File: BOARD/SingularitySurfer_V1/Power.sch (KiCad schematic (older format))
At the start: 32 parts, among them J1 USB_B_Micro, SW1 SW_DIP_x01, U1 BD81870EFV, U2 MIC5504-3.3YM5, U3 TLV70212_SOT23-5

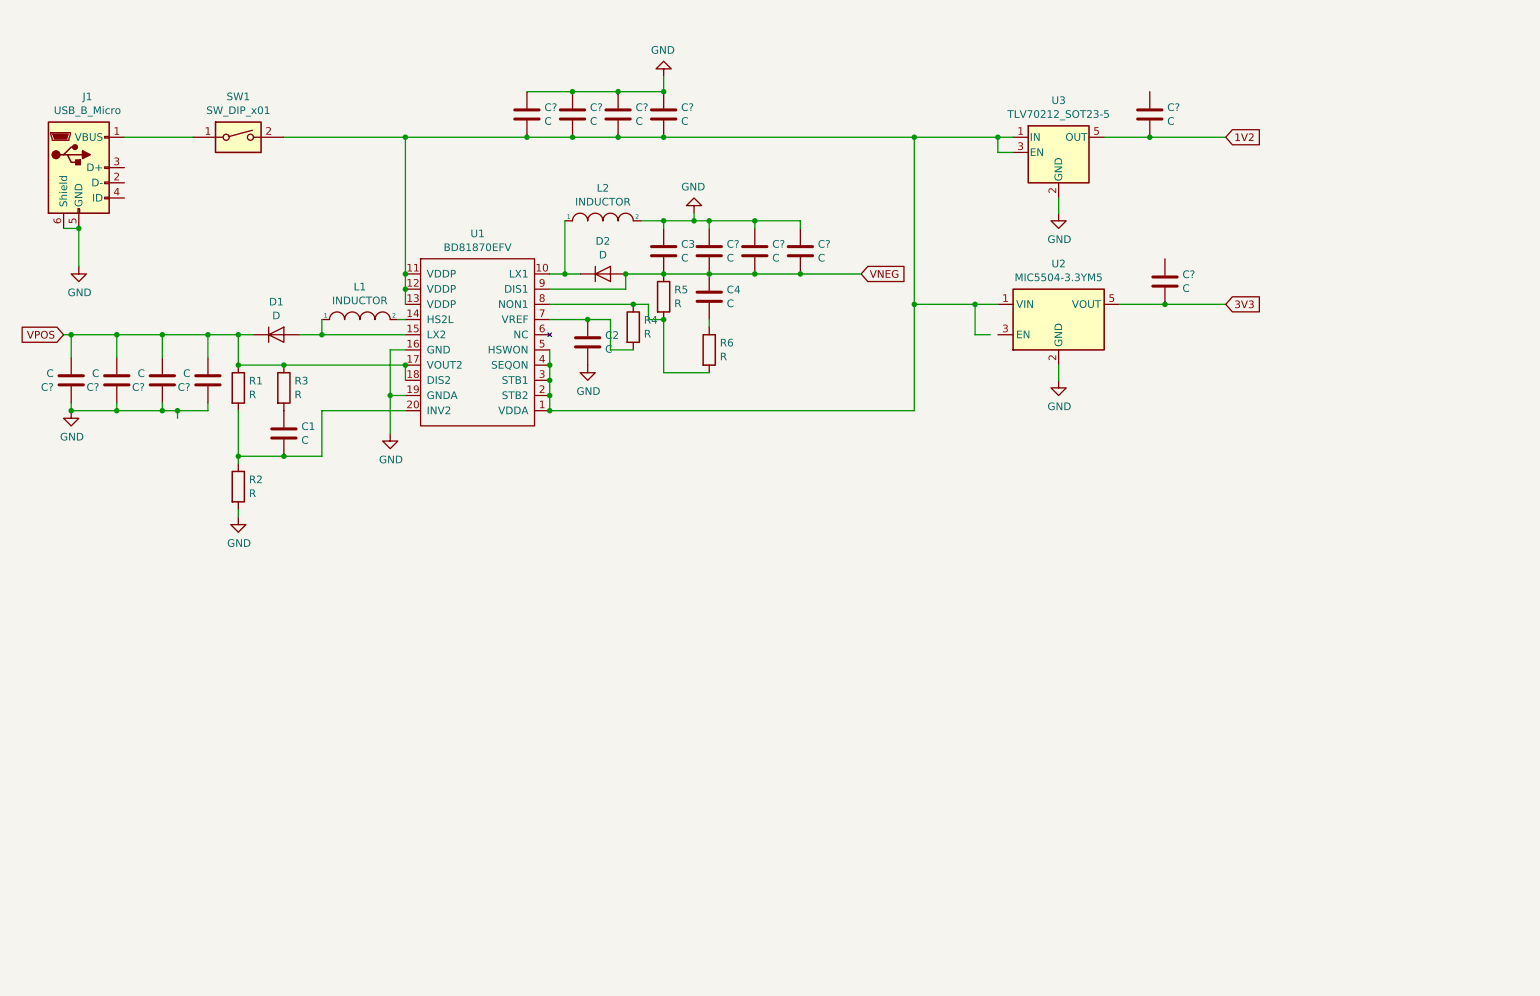
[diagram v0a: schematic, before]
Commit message: More work on final Schematic. Power, digital and output section close to final. No frontend yet.
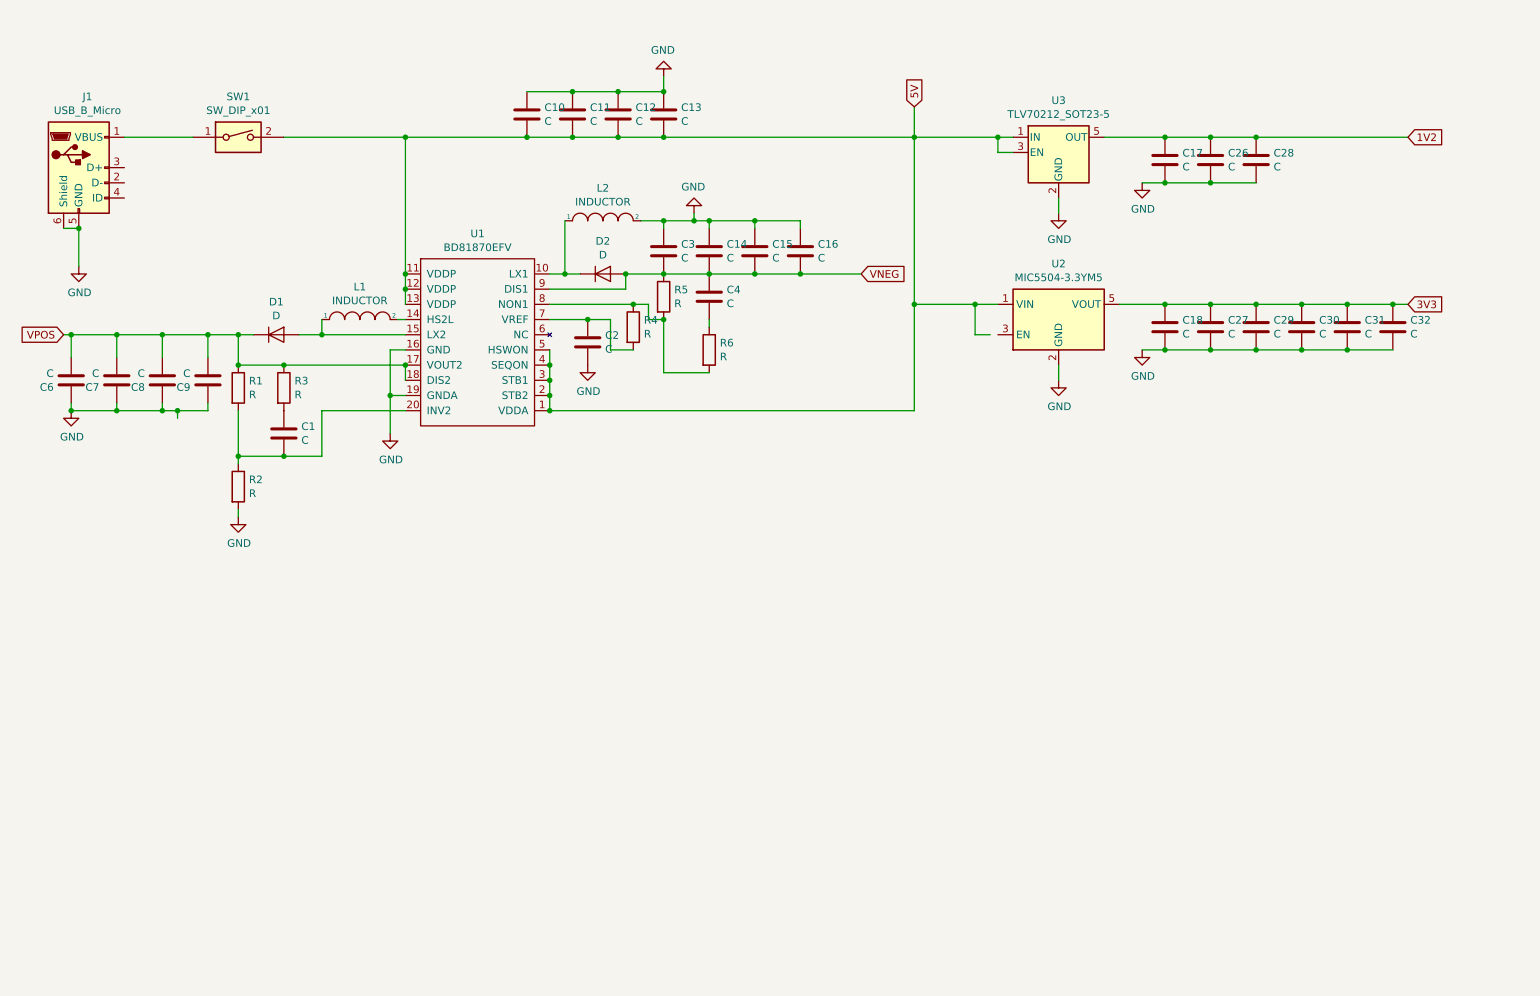
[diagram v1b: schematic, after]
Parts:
- added C26, C27, C28, C29, C30, C31, C32: C, symbol Device:C
- U1: footprint Button_Switch_THT:SW_CuK_JS202011AQN_DPDT_Angled -> Package_SO:SSOP-20_4.4x6.5mm_P0.65mm
- U2, U3: footprint Package_TO_SOT_SMD:SOT-23-5 -> Package_TO_SOT_SMD:SOT-23-5_HandSoldering
- gave numbers to parts that had none: 13
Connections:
- net 1V2: now also C17.1, C26.1, C28.1; no longer C17.2
- net 3V3: now also C18.1, C27.1, C29.1, C30.1, C31.1, C32.1; no longer C18.2
- net GND: now also C17.2, C18.2, C26.2, C27.2, C28.2, C29.2, C30.2, C31.2, C32.2
- net 5V: now reaches C10.2, C11.2, C12.2, C13.2, SW1.2, U1.1 (VDDA), U1.11 (VDDP), U1.12 (VDDP), U1.13 (VDDP), U1.2 (STB2), U1.3 (STB1), U1.4 (SEQON), U1.5 (HSWON), U2.1 (VIN), U3.1 (IN), U3.3 (EN)
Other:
- moved on the sheet: C17, C18

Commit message: Final Board schematic almost done and started on layout
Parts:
- added C43, C51: C, Capacitor_SMD:C_1206_3216Metric_Pad1.42x1.75mm_HandSolder, symbol Device:C
- added C44, C45, C46, C47, C48, C49, C50, C52, C53, C54, C55, C56: C, Capacitor_SMD:C_0805_2012Metric_Pad1.15x1.40mm_HandSolder, symbol Device:C
- added D16: D_Zener, Diode_SMD:D_SOD-323, symbol Device:D_Zener
- added D17: D_Schottky_x2_Serial_AKC, Package_TO_SOT_SMD:SOT-23, symbol Device:D_Schottky_x2_Serial_AKC
- added D3001: LED, LED_SMD:LED_0805_2012Metric_Pad1.15x1.40mm_HandSolder, symbol Device:LED
- added R35, R36, R37, R38: R, Resistor_SMD:R_0805_2012Metric_Pad1.15x1.40mm_HandSolder, symbol Device:R
- added U13: LT3032, Package_DFN_QFN:Linear_DE14MA, symbol Regulator_Linear:LT3032
- added U14: AP2114-1.8, Package_TO_SOT_SMD:TO-252-3_TabPin2, symbol SingularitySurfer:AP2114-1.8
- C1, C4: footprint (none) -> Capacitor_SMD:C_1206_3216Metric_Pad1.42x1.75mm_HandSolder
- C10, C11, C12, C13, C14, C15, C16, C17, C18, C2, C26, C27, C28, C29, C3, C30, C31, C32, C6, C7, C8, C9: footprint (none) -> Capacitor_SMD:C_0805_2012Metric_Pad1.15x1.40mm_HandSolder
- D1, D2: footprint (none) -> Diode_SMD:D_2010_5025Metric_Pad1.52x2.65mm_HandSolder
- L1, L2: footprint (none) -> Inductor_SMD:L_Taiyo-Yuden_NR-40xx_HandSoldering
- R1, R2, R3, R4, R5, R6: footprint (none) -> Resistor_SMD:R_0805_2012Metric_Pad1.15x1.40mm_HandSolder
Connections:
- net 5V: now also D16.1 (K), D3001.2 (A)
- net GND: now also C44.2, C45.2, C46.2, C47.2, C48.2, C49.2, C50.2, C52.2, C53.2, C54.2, C55.2, C56.2, D16.2 (A), D17.1 (A), D3001.1 (K), R36.1, R38.1, U13.4 (GND), U13.5 (GND), U14.2 (GND)
- net VPOS: now also U13.10 (~SHDNN), U13.12 (~SHDNP), U13.14 (INP)
- net VNEG: no longer names the net of C14.2, C15.2, C16.2, C3.2, C4.1, D2.2 (A), R5.1, U1.9 (DIS1)
- net VNEG: now also U13.6 (INN), U13.9 (INN)
- new net: R35.1, R36.2, U13.2 (ADJP)
- new net: C43.2, U13.3 (BYPP)
- new net: C51.2, U13.11 (BYPN)
- new net: R37.1, R38.2, U13.8 (ADJN)
- new net +8V: C43.1, C44.1, C46.1, C48.1, C49.1, C50.1, R35.2, U13.1 (OUTP), U14.1 (VIN)
- new net -8V: C51.1, C52.1, C53.1, C54.1, C55.1, C56.1, U13.7 (OUTN)
- new net A1V8: C45.1, C47.1, U14.3 (VOUT)
- no-connect marks 0 -> 1

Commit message: SignularitiSurfer final boar almost donegit status! Fuuuak this is getting rediculous...
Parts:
- added C57, C58, C59, C60, C64: C, Capacitor_SMD:C_0805_2012Metric_Pad1.15x1.40mm_HandSolder, symbol Device:C
- added C61, C62, C63: C, Capacitor_SMD:C_0402_1005Metric, symbol Device:C
- added J13, J14: Conn_01x03, Connector_JST:JST_EH_B3B-EH-A_1x03_P2.50mm_Vertical, symbol Connector_Generic:Conn_01x03
- added R39: R, Resistor_SMD:R_0805_2012Metric_Pad1.15x1.40mm_HandSolder, symbol Device:R
- added TP1, TP2, TP3, TP4, TP5, TP6, TP7, TP8: TestPoint, TestPoint:TestPoint_Keystone_5000-5004_Miniature, symbol Connector:TestPoint
- C30, C52: footprint Capacitor_SMD:C_0805_2012Metric_Pad1.15x1.40mm_HandSolder -> Capacitor_SMD:C_0402_1005Metric
- U13: footprint Package_DFN_QFN:Linear_DE14MA -> SingularitySurfer:DFN-14-1EP_split_bottom_pad_3x4mm_P0.5mm_EP1.7x3.3mm
- renumbered D3001 to D18
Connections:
- net +8V: now also C59.1, J13.1 (Pin_1), J14.1 (Pin_1), TP4.1
- net -8V: now also R37.2, C60.1, J13.3 (Pin_3), J14.3 (Pin_3), TP7.1; no longer C52.1
- net 1V2: now also C52.1, C62.1, TP8.1
- net 3V3: now also C61.1, C63.1, C64.1, TP6.1
- net 5V: now also D17.3 (common), C57.2, C58.2
- net GND: now also C57.1, C58.1, C59.2, C60.2, C61.2, C62.2, C63.2, C64.2, J13.2 (Pin_2), J14.2 (Pin_2), R39.1; no longer D18.1 (K)
- net VPOS: now also TP1.1
- net at J1.1 (VBUS), SW1.1: now also TP2.1
- net VNEG: now reaches C14.2, C15.2, C16.2, C3.2, C4.1, D2.2 (A), R5.1, U1.9 (DIS1), U13.6 (INN), U13.9 (INN)
- net VNEG: now also TP5.1
- net A1V8 renamed 1V8
- net 1V8: now also TP3.1
- new net: D18.1 (K), R39.2
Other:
- moved on the sheet: C44, C45, C46, C47, C48, C49, C50, U14

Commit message: Final board done, plotted and in production. Started on LCD driver, already working with scrolling HI :)
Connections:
- net 5V: now also U2.3 (EN)
- no-connect marks 1 -> 4
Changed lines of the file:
@@
 	7000 2700 7000 3400
-Wire Wire Line
-	7500 2900 7400 2900
 Wire Wire Line
 	7400 2900 7400 2700
@@
 $EndComp
 Wire Wire Line
-	6650 2500 6650 5150
-Wire Wire Line
 	1150 2900 1150 5250
 Wire Wire Line
@@
 Text Label 1150 5250 0    50   ~ 0
 VPOS
-Text GLabel 6350 5350 0    50   Input ~ 0
-VPOS
-Wire Wire Line
-	6350 5350 6650 5350
 $Comp
 L power:GND #PWR0151
@@
 	10450 3000 10750 3000
 Connection ~ 10450 3000
+Wire Wire Line
+	6650 2500 6650 5150
+Wire Wire Line
+	6650 5350 6650 6000
+Wire Wire Line
+	6650 6000 1150 6000
+Wire Wire Line
+	1150 6000 1150 5250
+Connection ~ 1150 5250
+NoConn ~ 1800 1800
+NoConn ~ 1800 1900
+NoConn ~ 1800 2000
+Wire Wire Line
+	7400 2900 7550 2900
 $EndSCHEMATC

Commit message: idiot me forgot to push final changes half a year ago.. Fixed code: filter constant 3 bit, filter downsampling factor and some mics.   Converted KiCad stuff to new version
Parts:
- U1: symbol SingularitySurfer:BD81870EFV -> SingularitySurfer_V1-rescue:BD81870EFV-SingularitySurfer
- U14: symbol SingularitySurfer:AP2114-1.8 -> SingularitySurfer_V1-rescue:AP2114-1.8-SingularitySurfer
- U3: symbol Regulator_Linear:TLV70212_SOT23-5 -> SingularitySurfer_V1-rescue:TLV70212_SOT23-5-Regulator_Linear
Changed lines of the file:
@@
 EESchema Schematic File Version 4
-LIBS:SingularitySurfer_V1-cache
 EELAYER 30 0
 EELAYER END
@@
 Connection ~ 1500 2200
 $Comp
-L SingularitySurfer:BD81870EFV U1
+L SingularitySurfer_V1-rescue:BD81870EFV-SingularitySurfer U1
 U 1 1 5D892AFE
 P 4100 2900
@@
 $EndComp
 $Comp
-L Regulator_Linear:TLV70212_SOT23-5 U3
+L SingularitySurfer_V1-rescue:TLV70212_SOT23-5-Regulator_Linear U3
 U 1 1 5D8B29B2
 P 7950 1700
@@
 	9550 5450 9300 5450
 $Comp
-L SingularitySurfer:AP2114-1.8 U14
+L SingularitySurfer_V1-rescue:AP2114-1.8-SingularitySurfer U14
 U 1 1 5DAF3A03
 P 5000 4250
